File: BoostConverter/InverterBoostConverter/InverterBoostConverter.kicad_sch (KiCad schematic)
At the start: 0 parts

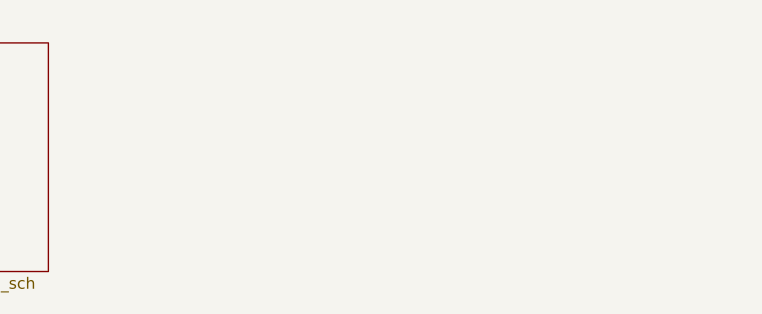
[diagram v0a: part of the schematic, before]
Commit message: Update boost converter, add inverter
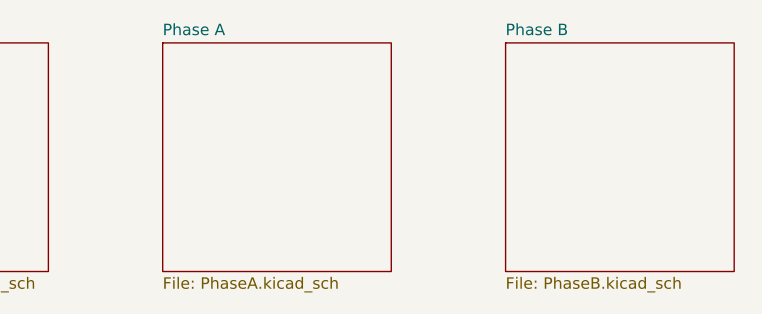
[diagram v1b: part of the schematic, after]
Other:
- added sheet Phase A (PhaseA.kicad_sch)
- added sheet Phase B (PhaseB.kicad_sch)
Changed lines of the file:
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@@
+	)
+	(sheet
+		(at 215.9 25.4)
+		(size 25.4 25.4)
+		(fields_autoplaced yes)
+		(stroke
+			(width 0.1524)
+			(type solid)
+		)
+		(fill
+			(color 0 0 0 0.0000)
+		)
+		(property "Sheetname" "Phase B"
+			(at 215.9 24.6884 0)
+			(effects
+				(font
+					(size 1.27 1.27)
+				)
+				(justify left bottom)
+			)
+		)
+		(property "Sheetfile" "PhaseB.kicad_sch"
+			(at 215.9 51.3846 0)
+			(effects
+				(font
+					(size 1.27 1.27)
+				)
+				(justify left top)
+			)
+		)
+		(instances
+			(project "InverterBoostConverter"
+				(path "/2b0bf6ef-6fb8-4b0f-8d72-c07d92ef1505"
+					(page "7")
+				)
+			)
+		)
 	)
 	(sheet
@@
 				)
 			)
+		)
+	)
+	(sheet
+		(at 177.8 25.4)
+		(size 25.4 25.4)
+		(fields_autoplaced yes)
+		(stroke
+			(width 0.1524)
+			(type solid)
+		)
+		(fill
+			(color 0 0 0 0.0000)
+		)
+		(property "Sheetname" "Phase A"
+			(at 177.8 24.6884 0)
+			(effects
+				(font
+					(size 1.27 1.27)
+				)
+				(justify left bottom)
+			)
+		)
+		(property "Sheetfile" "PhaseA.kicad_sch"
+			(at 177.8 51.3846 0)
+			(effects
+				(font
+					(size 1.27 1.27)
+				)
+				(justify left top)
+			)
+		)
+		(instances
+			(project "InverterBoostConverter"
+				(path "/2b0bf6ef-6fb8-4b0f-8d72-c07d92ef1505"
+					(page "6")
+				)
+			)
